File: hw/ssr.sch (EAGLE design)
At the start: 86 parts, among them T1 BC328, T2 BC328, T3 BC328, T4 BC328, T5 BC328

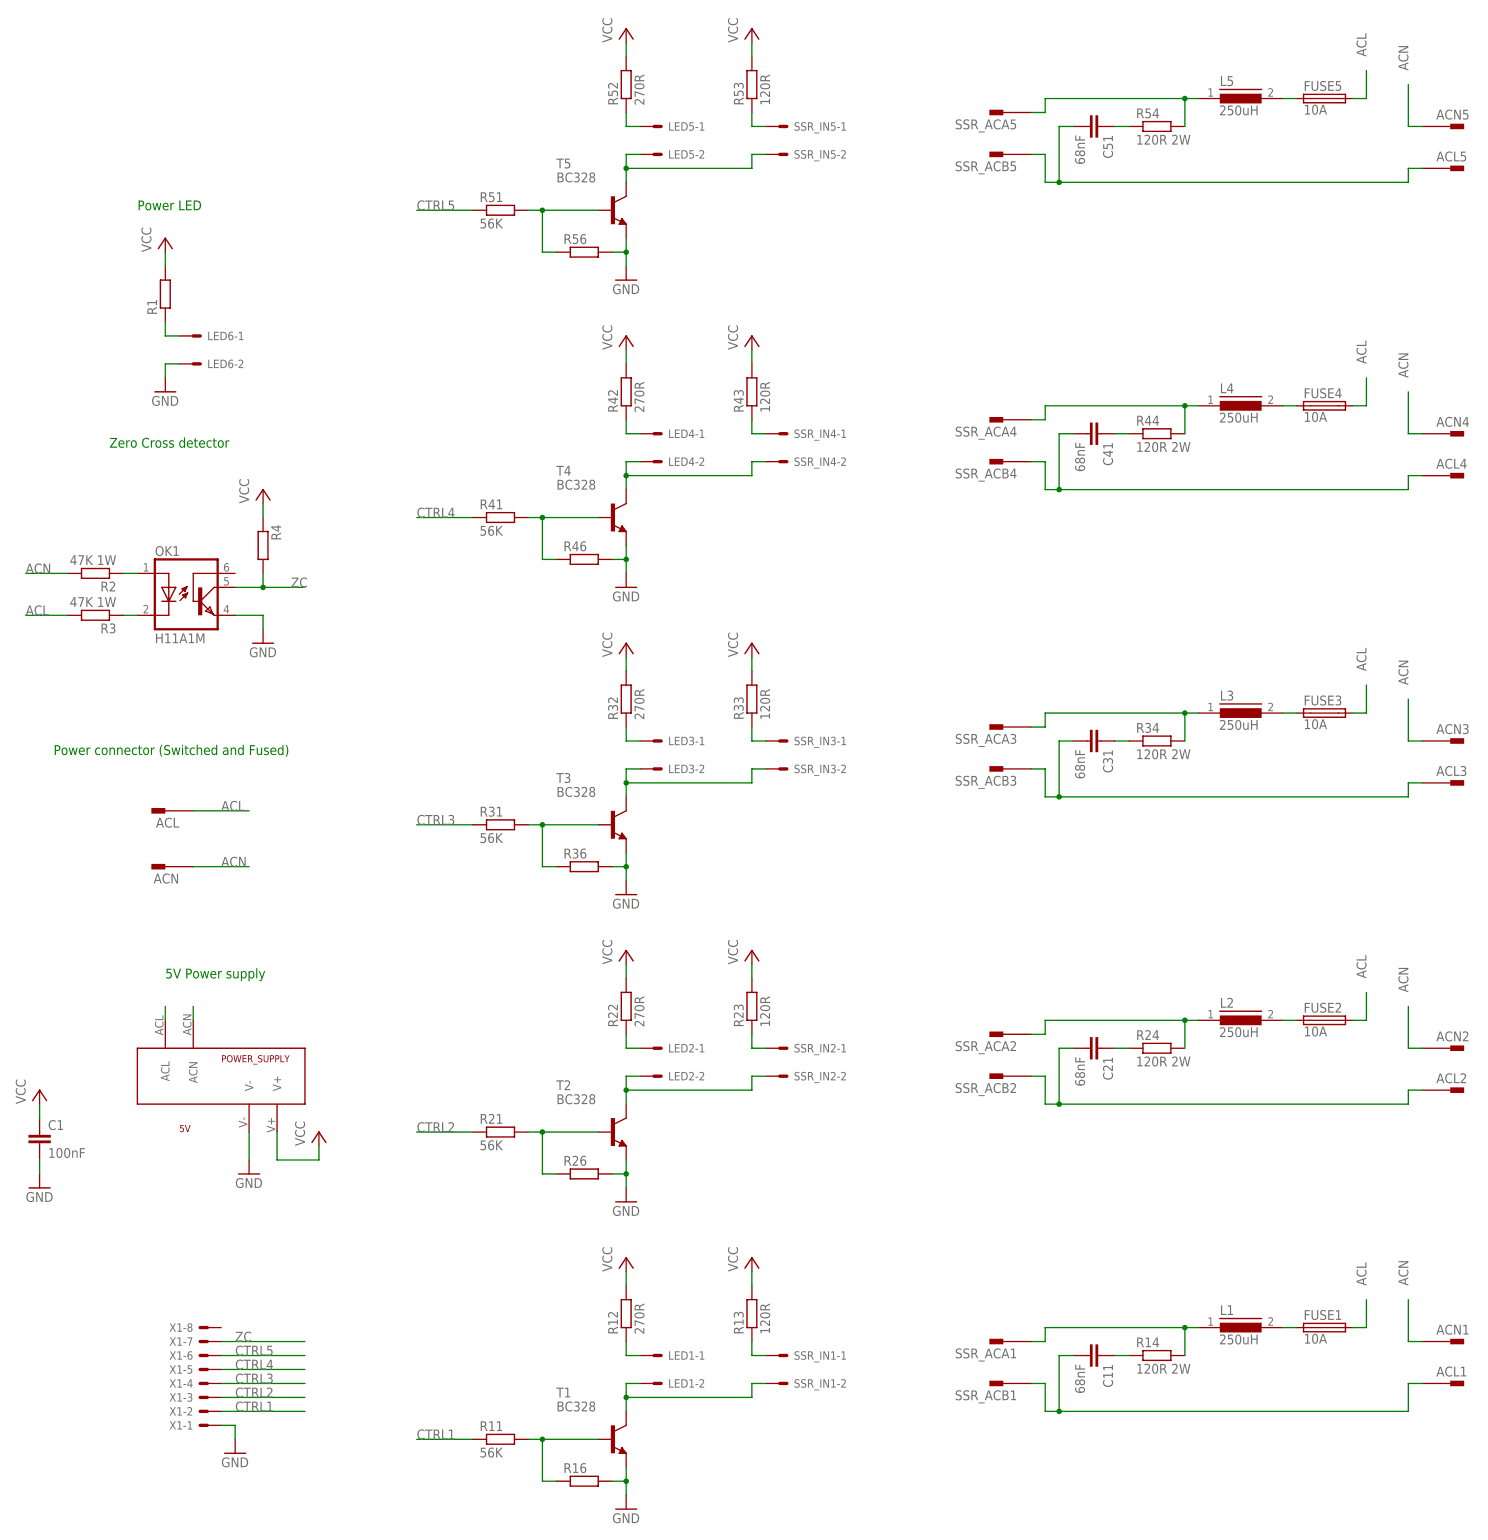
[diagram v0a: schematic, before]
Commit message: Adapt schematic and board layout according to new parts.
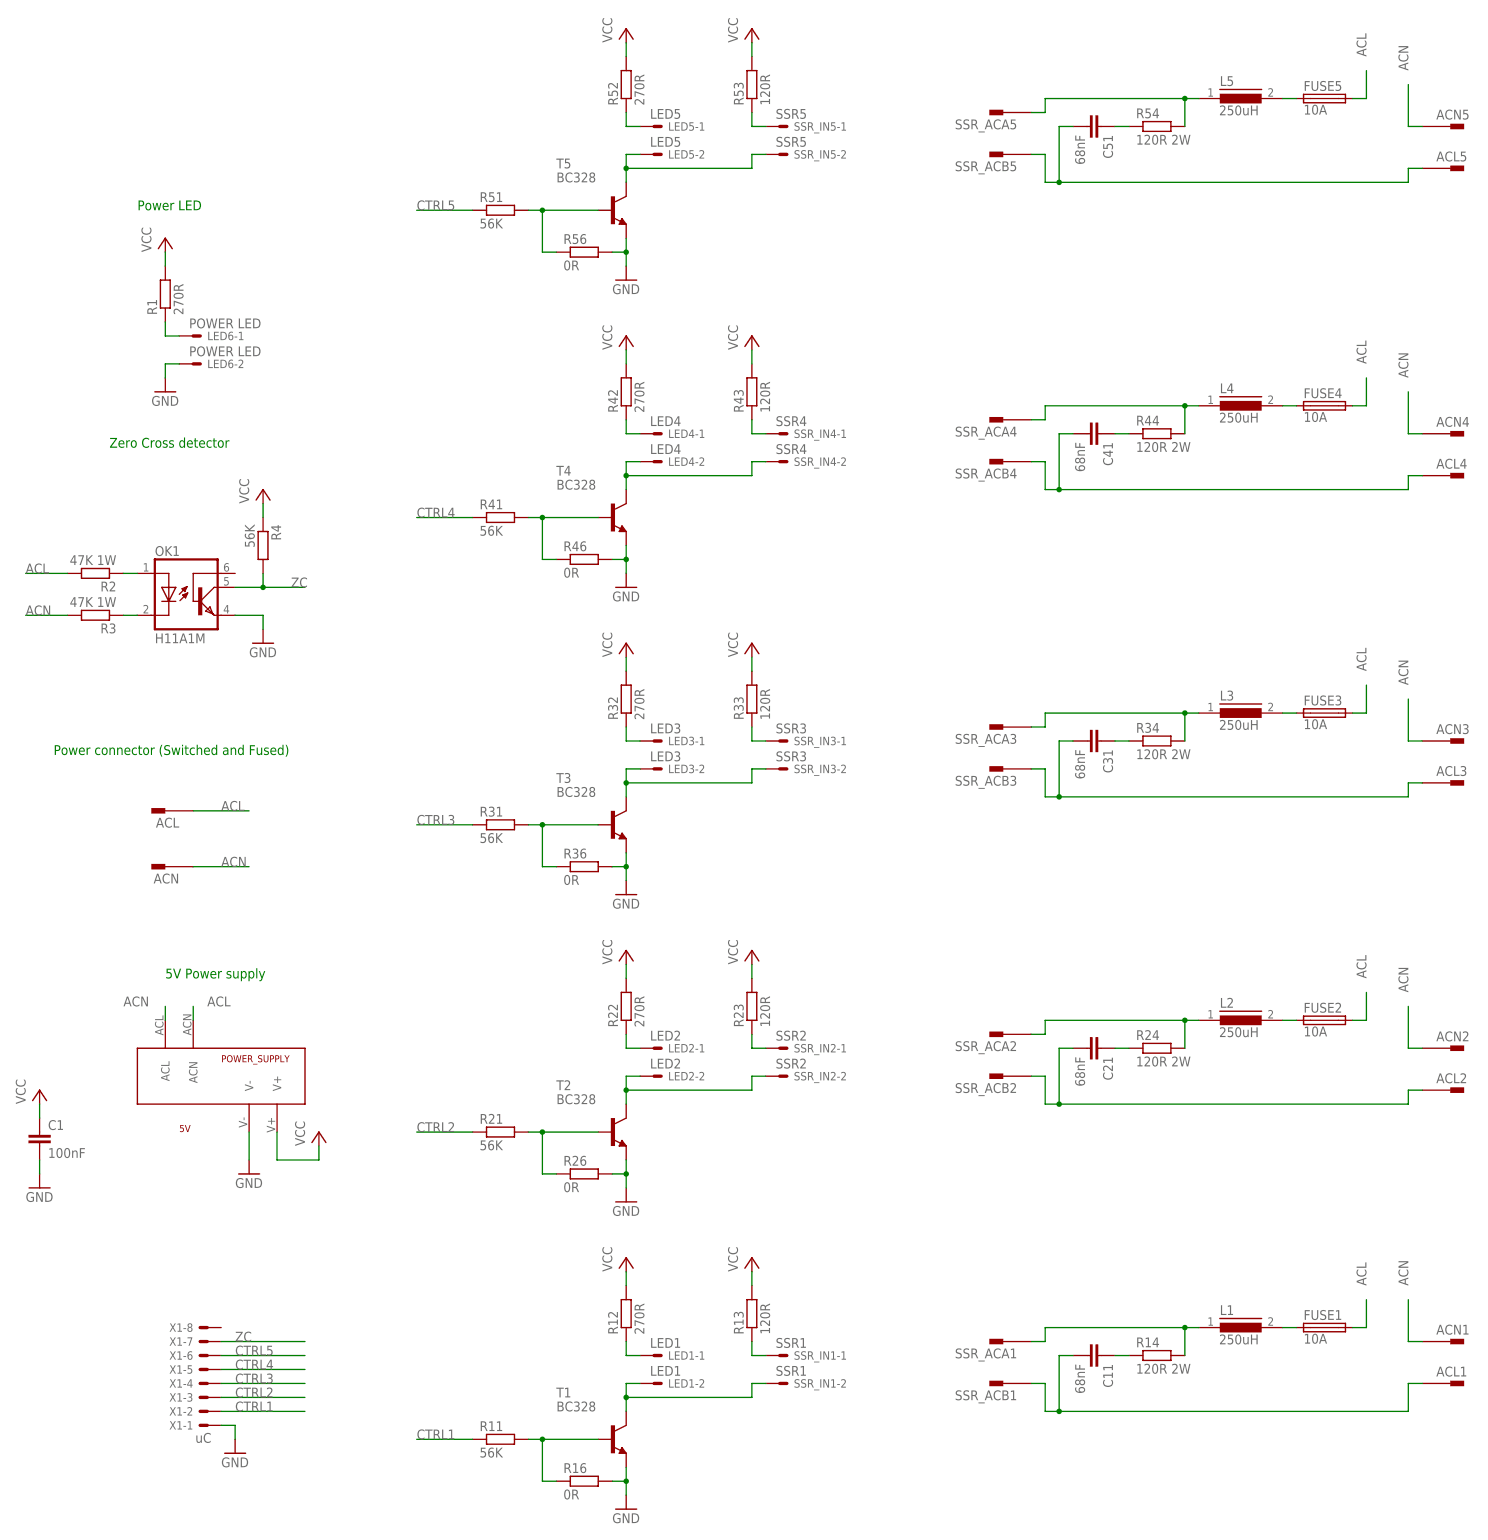
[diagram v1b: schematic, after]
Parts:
- LED1: value (none) -> LED1
- LED2: value (none) -> LED2
- LED3: value (none) -> LED3
- LED4: value (none) -> LED4
- LED5: value (none) -> LED5
- LED6: value (none) -> POWER LED
- R1: value (none) -> 270R
- R16, R26, R36, R46, R56: value (none) -> 0R
- R2, R3: device parts:R-EU_0207/10 -> resistor:R-EU_0309/12
- R4: value (none) -> 56K
- SSR_IN1: value (none) -> SSR1
- SSR_IN2: value (none) -> SSR2
- SSR_IN3: value (none) -> SSR3
- SSR_IN4: value (none) -> SSR4
- SSR_IN5: value (none) -> SSR5
- X1: value (none) -> uC
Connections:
- net ACL: now also R2.2; no longer R3.2
- net ACN: now also R3.2; no longer R2.2
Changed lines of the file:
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@@
 <part name="GND6" library="supply1" deviceset="GND" device=""/>
 <part name="GND7" library="supply1" deviceset="GND" device=""/>
-<part name="SSR_IN1" library="con-molex" deviceset="KK-156-2" device=""/>
-<part name="LED1" library="con-molex" deviceset="KK-156-2" device=""/>
-<part name="X1" library="con-molex" deviceset="KK-156-8" device=""/>
+<part name="SSR_IN1" library="con-molex" deviceset="KK-156-2" device="" value="SSR1"/>
+<part name="LED1" library="con-molex" deviceset="KK-156-2" device="" value="LED1"/>
+<part name="X1" library="con-molex" deviceset="KK-156-8" device="" value="uC"/>
 <part name="FUSE1" library="fuse" deviceset="FUSE" device="SH22,5" value="10A"/>
 <part name="R14" library="resistor" deviceset="R-EU_" device="0617/22" value="120R 2W"/>
@@
 <part name="ACN" library="parts" deviceset="PIN2" device="F061.080"/>
 <part name="OK1" library="optocoupler" deviceset="H11A*?M" device="" technology="1"/>
-<part name="R2" library="parts" deviceset="R-EU_" device="0207/10" value="47K 1W"/>
-<part name="R3" library="parts" deviceset="R-EU_" device="0207/10" value="47K 1W"/>
-<part name="R4" library="parts" deviceset="R-EU_" device="0207/10"/>
+<part name="R2" library="resistor" deviceset="R-EU_" device="0309/12" value="47K 1W"/>
+<part name="R3" library="resistor" deviceset="R-EU_" device="0309/12" value="47K 1W"/>
+<part name="R4" library="parts" deviceset="R-EU_" device="0207/10" value="56K"/>
 <part name="SSR_ACA1" library="parts" deviceset="PIN2" device="F061.080"/>
 <part name="SSR_ACB1" library="parts" deviceset="PIN2" device="F061.080"/>
@@
 <part name="P+8" library="supply1" deviceset="VCC" device=""/>
 <part name="GND3" library="supply1" deviceset="GND" device=""/>
-<part name="SSR_IN2" library="con-molex" deviceset="KK-156-2" device=""/>
-<part name="LED2" library="con-molex" deviceset="KK-156-2" device=""/>
+<part name="SSR_IN2" library="con-molex" deviceset="KK-156-2" device="" value="SSR2"/>
+<part name="LED2" library="con-molex" deviceset="KK-156-2" device="" value="LED2"/>
 <part name="FUSE2" library="fuse" deviceset="FUSE" device="SH22,5" value="10A"/>
 <part name="R24" library="resistor" deviceset="R-EU_" device="0617/22" value="120R 2W"/>
@@
 <part name="P+10" library="supply1" deviceset="VCC" device=""/>
 <part name="GND8" library="supply1" deviceset="GND" device=""/>
-<part name="SSR_IN3" library="con-molex" deviceset="KK-156-2" device=""/>
-<part name="LED3" library="con-molex" deviceset="KK-156-2" device=""/>
+<part name="SSR_IN3" library="con-molex" deviceset="KK-156-2" device="" value="SSR3"/>
+<part name="LED3" library="con-molex" deviceset="KK-156-2" device="" value="LED3"/>
 <part name="FUSE3" library="fuse" deviceset="FUSE" device="SH22,5" value="10A"/>
 <part name="R34" library="resistor" deviceset="R-EU_" device="0617/22" value="120R 2W"/>
@@
 <part name="P+12" library="supply1" deviceset="VCC" device=""/>
 <part name="GND9" library="supply1" deviceset="GND" device=""/>
-<part name="SSR_IN4" library="con-molex" deviceset="KK-156-2" device=""/>
-<part name="LED4" library="con-molex" deviceset="KK-156-2" device=""/>
+<part name="SSR_IN4" library="con-molex" deviceset="KK-156-2" device="" value="SSR4"/>
+<part name="LED4" library="con-molex" deviceset="KK-156-2" device="" value="LED4"/>
 <part name="FUSE4" library="fuse" deviceset="FUSE" device="SH22,5" value="10A"/>
 <part name="R44" library="resistor" deviceset="R-EU_" device="0617/22" value="120R 2W"/>
@@
 <part name="P+14" library="supply1" deviceset="VCC" device=""/>
 <part name="GND10" library="supply1" deviceset="GND" device=""/>
-<part name="SSR_IN5" library="con-molex" deviceset="KK-156-2" device=""/>
-<part name="LED5" library="con-molex" deviceset="KK-156-2" device=""/>
+<part name="SSR_IN5" library="con-molex" deviceset="KK-156-2" device="" value="SSR5"/>
+<part name="LED5" library="con-molex" deviceset="KK-156-2" device="" value="LED5"/>
 <part name="FUSE5" library="fuse" deviceset="FUSE" device="SH22,5" value="10A"/>
 <part name="R54" library="resistor" deviceset="R-EU_" device="0617/22" value="120R 2W"/>
@@
 <part name="SSR_ACA5" library="parts" deviceset="PIN2" device="F061.080"/>
 <part name="SSR_ACB5" library="parts" deviceset="PIN2" device="F061.080"/>
-<part name="R1" library="parts" deviceset="R-EU_" device="0207/10"/>
-<part name="LED6" library="con-molex" deviceset="KK-156-2" device=""/>
+<part name="R1" library="parts" deviceset="R-EU_" device="0207/10" value="270R"/>
+<part name="LED6" library="con-molex" deviceset="KK-156-2" device="" value="POWER LED"/>
 <part name="P+5" library="supply1" deviceset="VCC" device=""/>
 <part name="GND2" library="supply1" deviceset="GND" device=""/>
-<part name="R16" library="parts" deviceset="R-EU_" device="0207/10"/>
-<part name="R26" library="parts" deviceset="R-EU_" device="0207/10"/>
-<part name="R36" library="parts" deviceset="R-EU_" device="0207/10"/>
-<part name="R46" library="parts" deviceset="R-EU_" device="0207/10"/>
-<part name="R56" library="parts" deviceset="R-EU_" device="0207/10"/>
+<part name="R16" library="parts" deviceset="R-EU_" device="0207/10" value="0R"/>
+<part name="R26" library="parts" deviceset="R-EU_" device="0207/10" value="0R"/>
+<part name="R36" library="parts" deviceset="R-EU_" device="0207/10" value="0R"/>
+<part name="R46" library="parts" deviceset="R-EU_" device="0207/10" value="0R"/>
+<part name="R56" library="parts" deviceset="R-EU_" device="0207/10" value="0R"/>
 <part name="GND4" library="supply1" deviceset="GND" device=""/>
 <part name="P+6" library="supply1" deviceset="VCC" device=""/>
@@
 </segment>
 <segment>
-<pinref part="R3" gate="G$1" pin="2"/>
-<wire x1="5.08" y1="177.8" x2="-2.54" y2="177.8" width="0.1524" layer="91"/>
-<label x="-2.54" y="177.8" size="1.778" layer="95"/>
-</segment>
-<segment>
 <pinref part="POWER_SUPPLY" gate="G$1" pin="ACN"/>
 <wire x1="27.94" y1="104.14" x2="27.94" y2="106.68" width="0.1524" layer="91"/>
+<label x="30.48" y="106.68" size="1.778" layer="95"/>
+</segment>
+<segment>
+<pinref part="R2" gate="G$1" pin="2"/>
+<wire x1="5.08" y1="185.42" x2="-2.54" y2="185.42" width="0.1524" layer="91"/>
+<label x="-2.54" y="185.42" size="1.778" layer="95"/>
 </segment>
 </net>
@@
 </segment>
 <segment>
-<pinref part="R2" gate="G$1" pin="2"/>
-<wire x1="5.08" y1="185.42" x2="-2.54" y2="185.42" width="0.1524" layer="91"/>
-<label x="-2.54" y="185.42" size="1.778" layer="95"/>
-</segment>
-<segment>
 <pinref part="POWER_SUPPLY" gate="G$1" pin="ACL"/>
 <wire x1="22.86" y1="104.14" x2="22.86" y2="106.68" width="0.1524" layer="91"/>
+<label x="15.24" y="106.68" size="1.778" layer="95"/>
+</segment>
+<segment>
+<pinref part="R3" gate="G$1" pin="2"/>
+<wire x1="5.08" y1="177.8" x2="-2.54" y2="177.8" width="0.1524" layer="91"/>
+<label x="-2.54" y="177.8" size="1.778" layer="95"/>
 </segment>
 </net>
@@
 </sheet>
 </sheets>
+<errors>
+</errors>
 </schematic>
 </drawing>
